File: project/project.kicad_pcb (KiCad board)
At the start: 2 copper layers, 72 x 26 mm, 11 parts, among them J1 IDC 2x8, U1 top, U2 mag

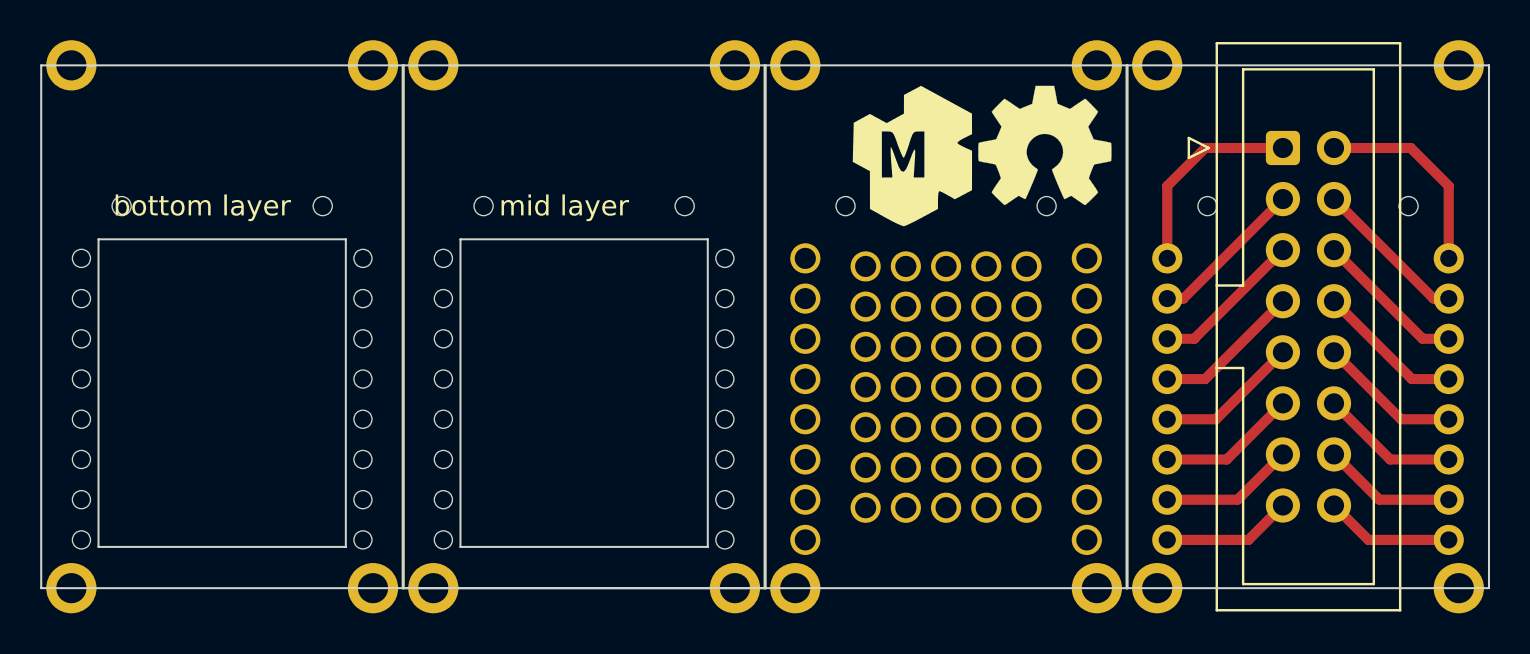
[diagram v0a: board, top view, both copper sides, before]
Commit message: small size adjustments and labels
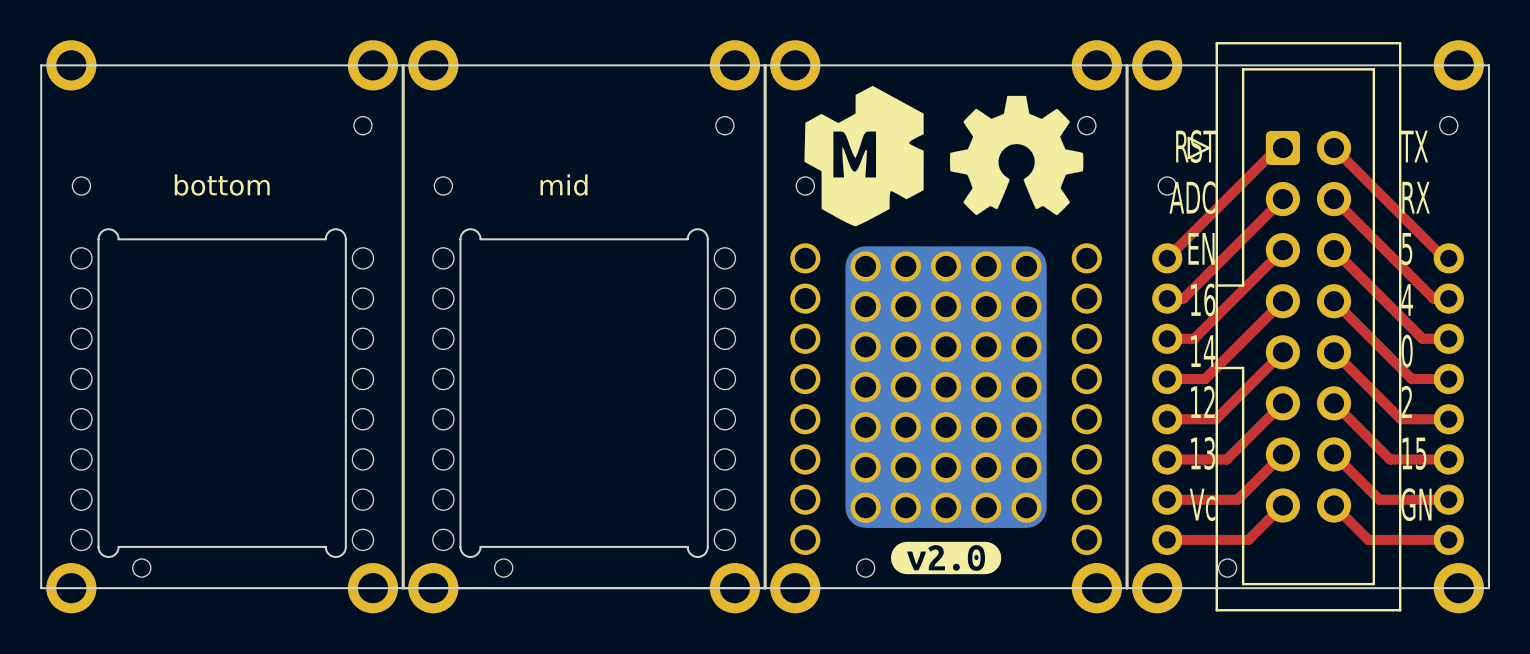
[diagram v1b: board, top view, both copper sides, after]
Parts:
- added kibuzzard-64235F14: G***, kibuzzard-64235F14, B.Cu at (121.5, 125.0)
- added kibuzzard-64235F4D: G***, kibuzzard-64235F4D, F.Cu at (157.5, 124.5)
- added kibuzzard-64235FFD: G***, kibuzzard-64235FFD, B.Cu at (180.5, 113.0)
- moved G2 2.41 mm to (153.0, 104.5)
- moved G1 1.49 mm to (161.0, 104.5)
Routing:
- net TX: track 10.1 -> 7.98 mm
- net RST: track 10.1 -> 8.03 mm
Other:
- outline, holes or cut-outs redrawn
- board text added: "RST ADC EN 16 14 12 13 Vc"
- board text added: "TX RX 5 4 0 2 15 GN"
